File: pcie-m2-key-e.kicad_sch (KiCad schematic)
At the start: 15 parts, among them P1 2199119-6

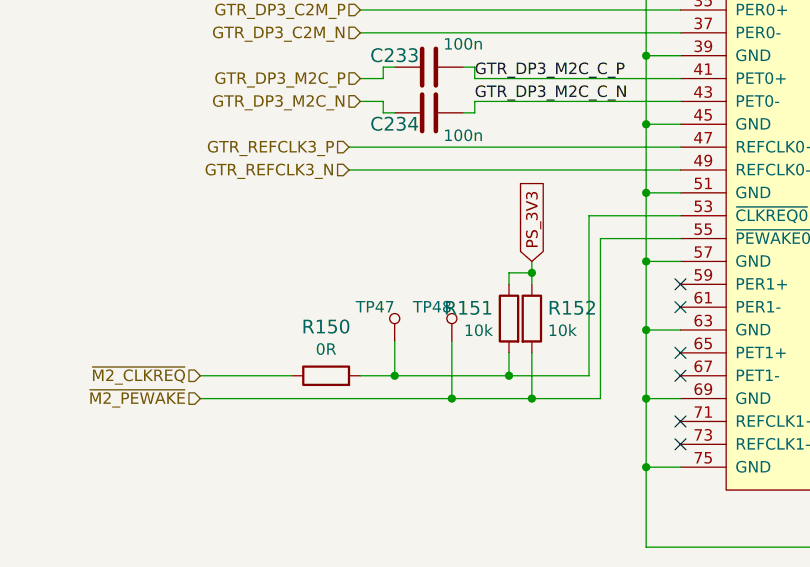
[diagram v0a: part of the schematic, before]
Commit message: Added cosmetic changes to schematics (e.g. position of labels, designators)
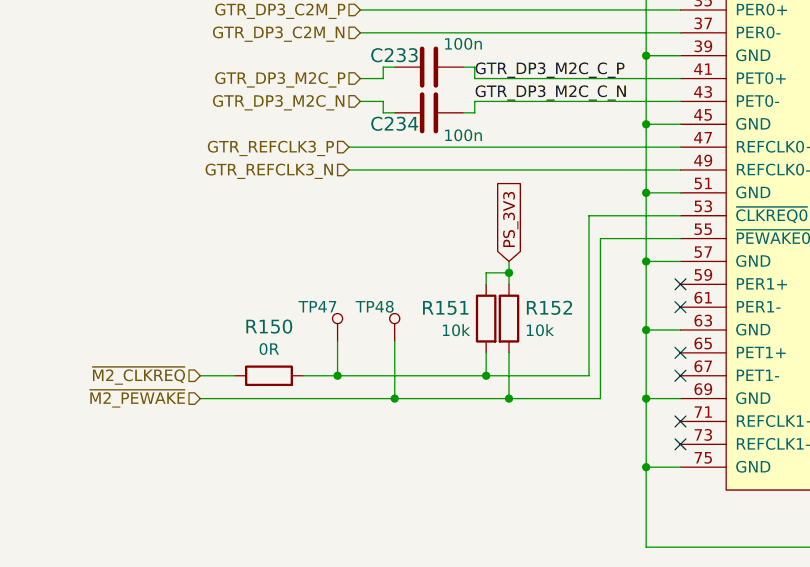
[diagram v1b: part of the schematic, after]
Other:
- moved on the sheet: R150, R151, R152, TP47, TP48

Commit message: Bump date and revision
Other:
- title: M.2 Key E -> Kria K26 Devboard
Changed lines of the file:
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@@
   (paper "A4")
   (title_block
-    (title "M.2 Key E")
-    (date "2022-07-25")
-    (rev "1.1.0")
+    (title "Kria K26 Devboard")
+    (date "2023-02-15")
+    (rev "1.1.1")
     (comment 1 "www.antmicro.com")
     (comment 2 "Antmicro Ltd.")

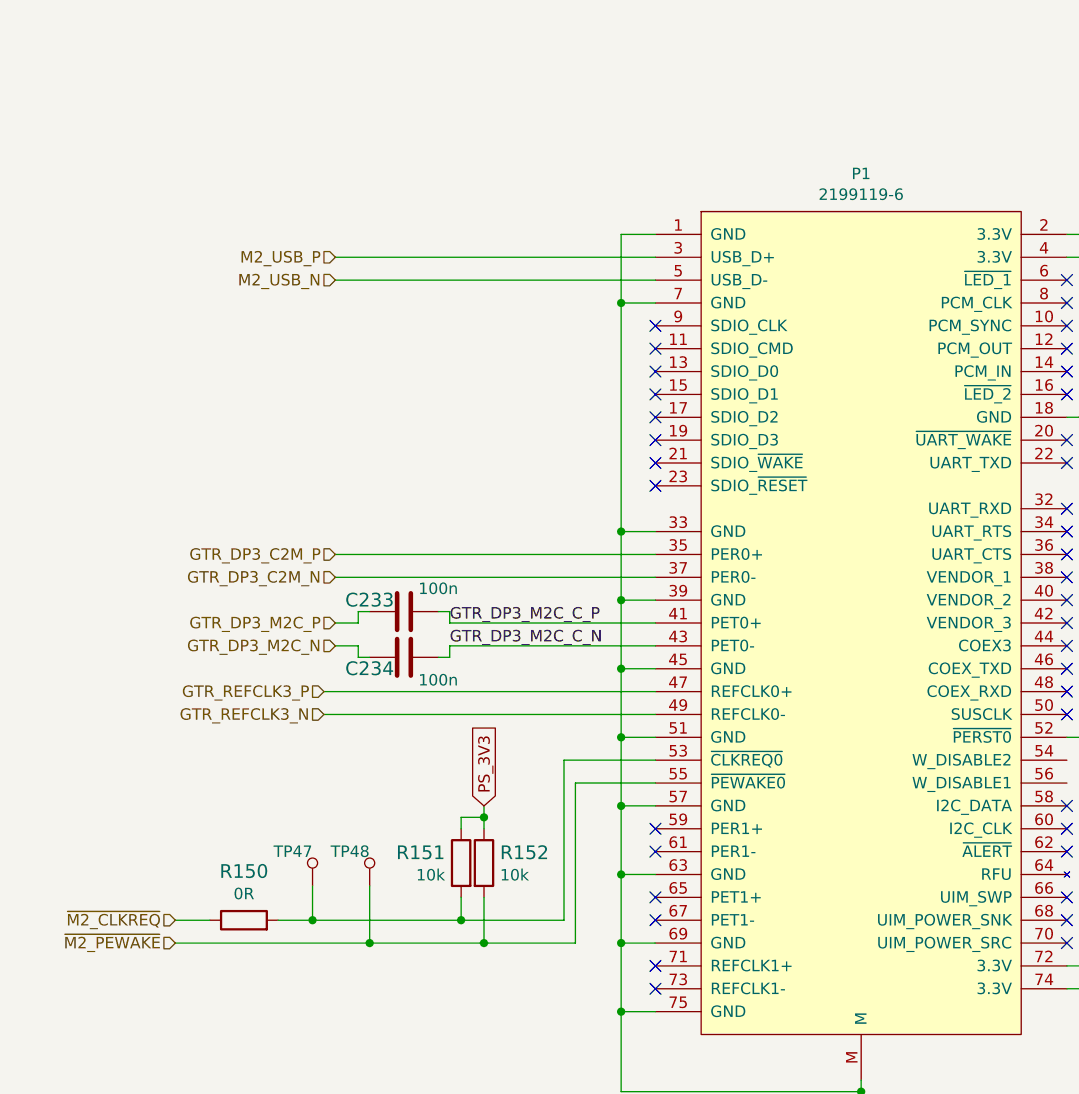
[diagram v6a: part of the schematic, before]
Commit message: Fix TX/RX cross on M.2 Key E
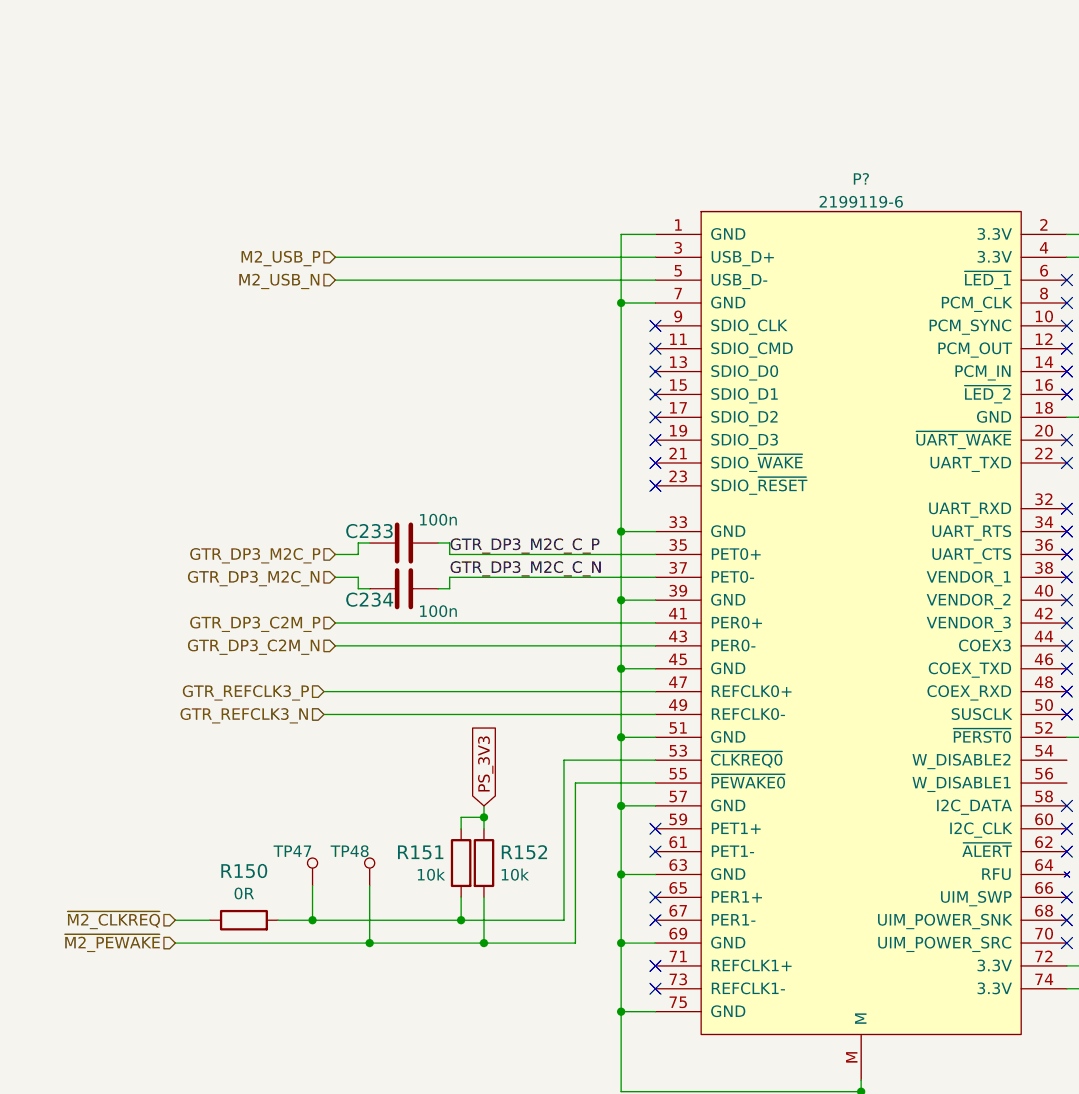
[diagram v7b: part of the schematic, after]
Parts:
- removed P1: 2199119-6, kria-k26-devboard-footprints:TE_1-2199119-6, symbol kria-k26-devboard:2199119-6
- added P?: 2199119-6, antmicro-footprints:TE_1-2199119-6, symbol antmicroPciConnectors:2199119-6
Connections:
- net GND: now also P?.1 (GND), P?.18 (GND), P?.33 (GND), P?.39 (GND), P?.45 (GND), P?.51 (GND), P?.57 (GND), P?.63 (GND), P?.69 (GND), P?.7 (GND), P?.75 (GND), P?.M
- net GTR_DP3_C2M_N: now also P?.43 (PER0-)
- net GTR_DP3_C2M_P: now also P?.41 (PER0+)
- net GTR_DP3_M2C_C_N: now also P?.37 (PET0-)
- net GTR_DP3_M2C_C_P: now also P?.35 (PET0+)
- net GTR_REFCLK3_N: now also P?.49 (REFCLK0-)
- net GTR_REFCLK3_P: now also P?.47 (REFCLK0+)
- net M2_USB_N: now also P?.5 (USB_D-)
- net M2_USB_P: now also P?.3 (USB_D+)
- net PS_3V3: now also P?.2 (3.3V), P?.4 (3.3V), P?.72 (3.3V), P?.74 (3.3V)
- net ~{M2_PERST}: now also P?.52 (~{PERST0})
- net ~{M2_PEWAKE}: now also P?.55 (~{PEWAKE0})
- net at R150.2, R151.2, TP47.1: now also P?.53 (~{CLKREQ0})
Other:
- moved on the sheet: C233, C234

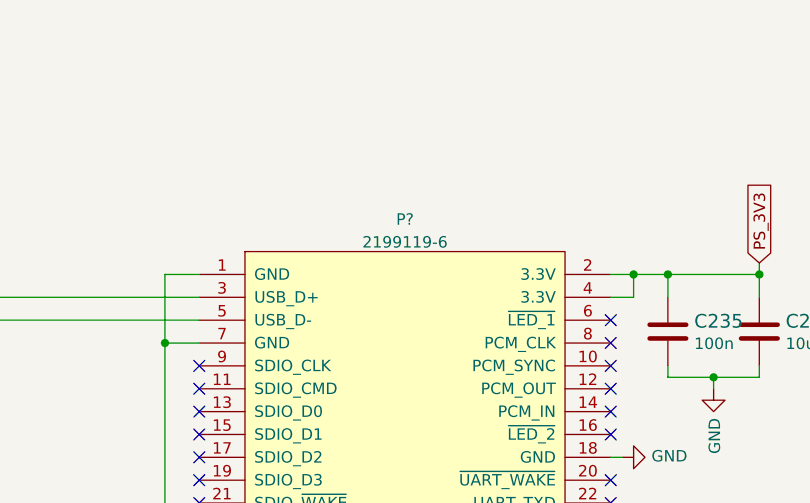
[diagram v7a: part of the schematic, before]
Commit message: Finish implementing review changes on schematic. Push to PCB
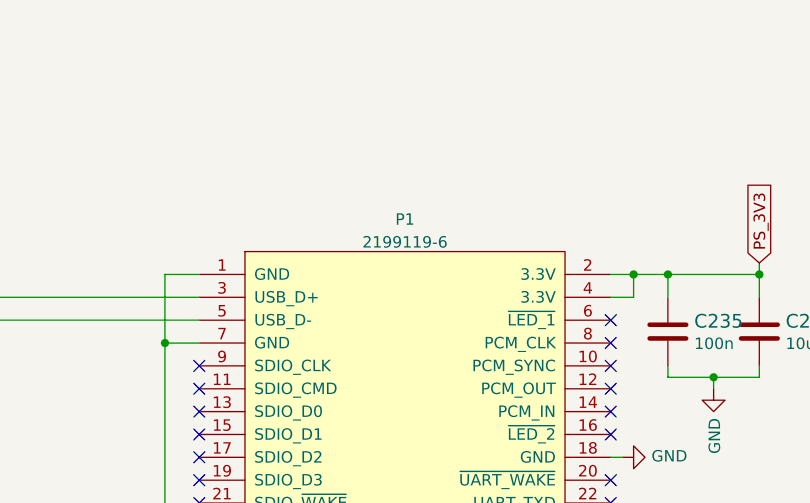
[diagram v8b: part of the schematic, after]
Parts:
- gave numbers to parts that had none: 1
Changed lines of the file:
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@@
   (title_block
     (title "Kria K26 Devboard")
-    (date "2023-02-15")
+    (date "2023-03-03")
     (rev "1.1.1")
     (comment 1 "www.antmicro.com")
@@
   (symbol (lib_id "antmicroPciConnectors:2199119-6") (at 152.4 73.66 0) (unit 1)
     (in_bom yes) (on_board yes) (fields_autoplaced)
-    (property "Reference" "P?" (id 0) (at 152.4 37.0672 0))
+    (property "Reference" "P1" (id 0) (at 152.4 37.0672 0))
     (property "Value" "2199119-6" (id 1) (at 152.4 39.6041 0))
     (property "Footprint" "antmicro-footprints:TE_1-2199119-6" (id 2) (at 152.4 59.69 0)
